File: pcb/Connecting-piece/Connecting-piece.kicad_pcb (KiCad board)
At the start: 2 copper layers, 66.4 x 24.5 mm, 22 parts, among them J1 Conn_01x08_Male, J10 Conn_01x01, J11 Conn_01x01, J12 Conn_01x01, J13 Conn_01x01, J14 Conn_01x01, J15 Conn_01x01, J16 Conn_01x01, J17 Conn_01x01, J18 Conn_01x01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

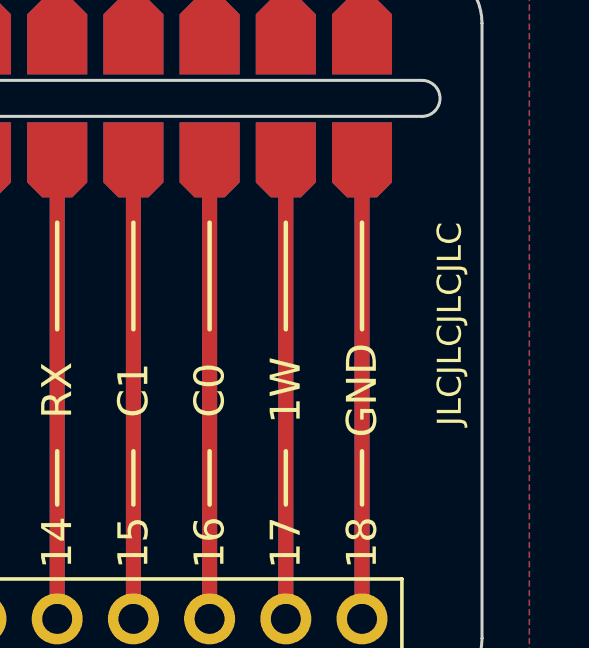
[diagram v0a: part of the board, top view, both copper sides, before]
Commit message: Remove JLCJLCJLCJLC String from all PCBs
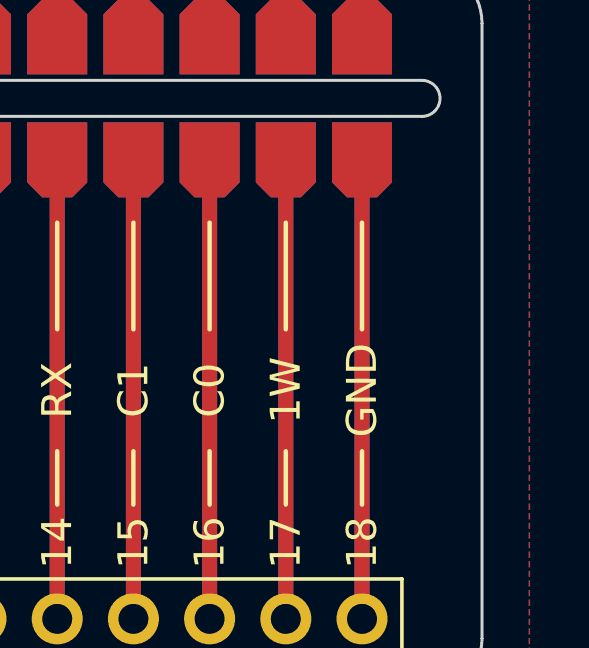
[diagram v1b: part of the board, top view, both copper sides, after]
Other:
- board text removed: "JLCJLCJLCJLC"
